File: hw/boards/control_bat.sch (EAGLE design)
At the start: 17 parts, among them U1 579-MCP1703T-3002ECB, U2 771-LPC824M201JDH20J, U3 888-XB24CZ7PIS-004

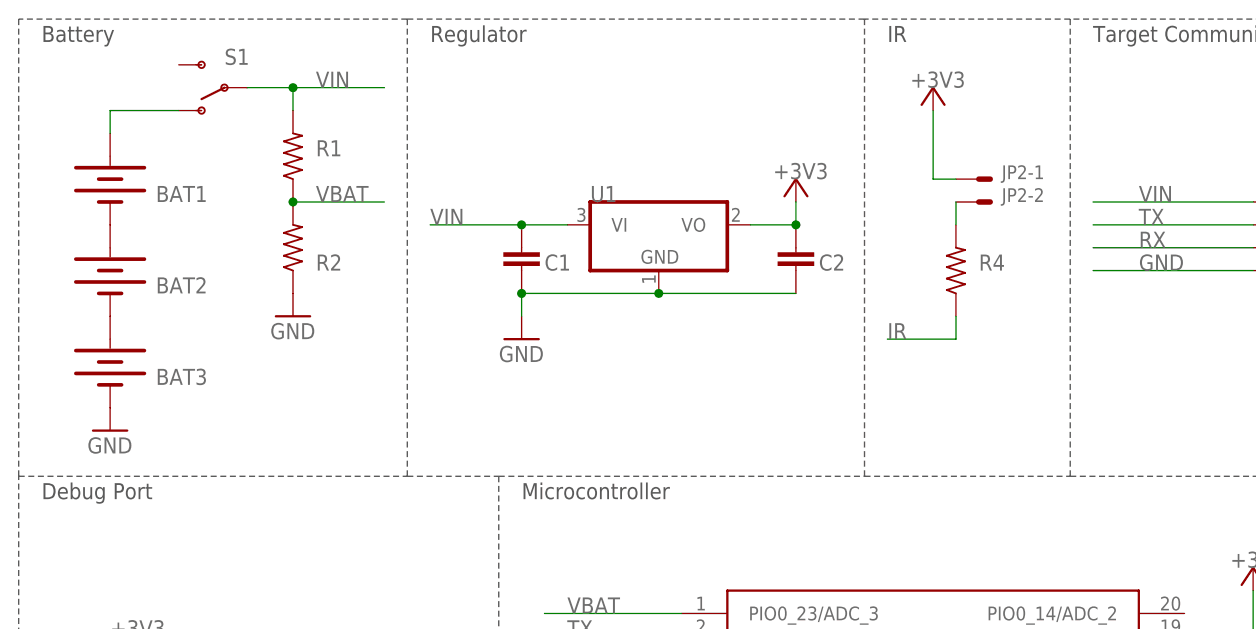
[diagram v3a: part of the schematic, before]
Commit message: Final fixes to the controller board.
This board will probably never be fabbed but I'm documenting the fixes made to hardware here for future reference.
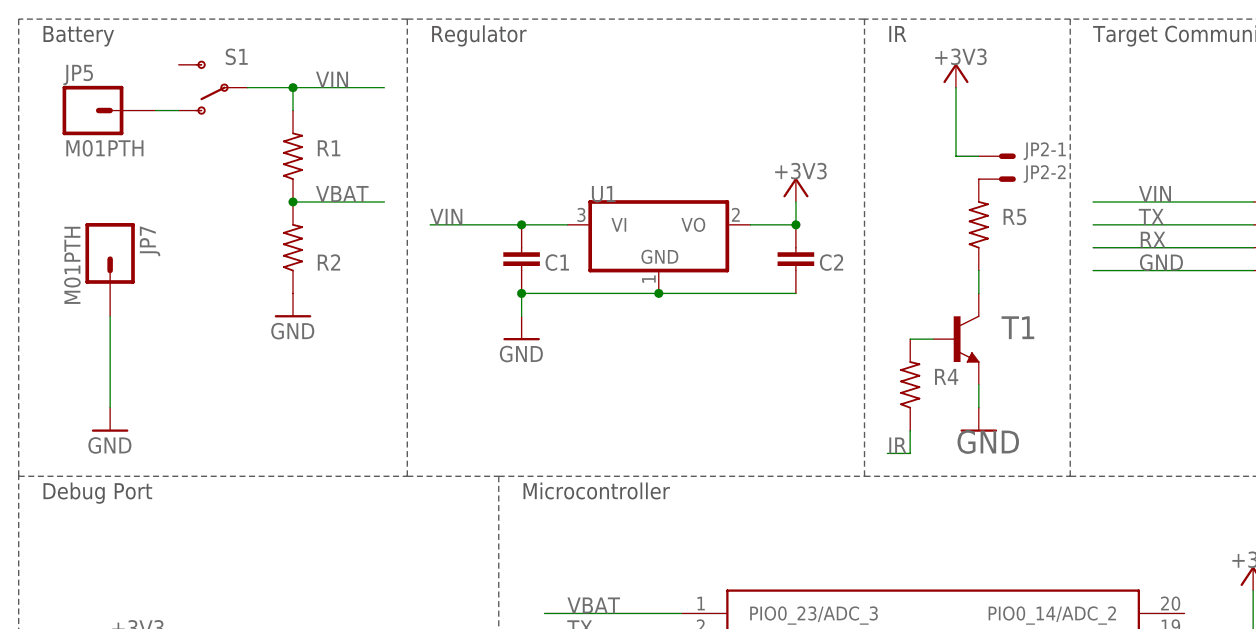
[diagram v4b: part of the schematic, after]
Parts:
- removed BAT1, BAT2, BAT3: 534-082, SparkFun-Electromechanical:BATTERYAAA-KIT
- added JP5, JP7: M01PTH, SparkFun-Connectors:M01PTH
- added R5: 71-CRCW0603-5.6-E3, rcl:R-US_R0603
- added T1: PMBT4401,215, transistor:MMBT4401LT1-NPN-SOT23-BEC
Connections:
- removed net N$2: BAT1.-, BAT2.+
- removed net N$3: BAT1.+, S1.O
- new net N$5: R5.1, T1.C
- new net N$6: R4.2, T1.B
- net GND: now also JP7.1, T1.E; no longer BAT3.-
- net N$1: now also JP5.1, S1.O; no longer BAT2.-, BAT3.+
- net N$4: now also R5.2; no longer R4.2
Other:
- moved on the sheet: JP2-1, JP2-2, R4
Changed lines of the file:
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@@
 <setting verticaltext="up"/>
 </settings>
-<grid distance="0.1" unitdist="inch" unit="inch" style="lines" multiple="1" display="no" altdistance="0.01" altunitdist="inch" altunit="inch"/>
+<grid distance="0.1" unitdist="inch" unit="inch" style="lines" multiple="1" display="yes" altdistance="0.01" altunitdist="inch" altunit="inch"/>
 <layers>
 <layer number="1" name="Top" color="4" fill="1" visible="no" active="no"/>
@@
 <part name="JP3" library="con-molex" deviceset="53?-04" device="398" value="798-DF134P125V20"/>
 <part name="JP1" library="torpedo" deviceset="FTSH-105" device="" value="FTSH-105-01-L"/>
-<part name="BAT3" library="SparkFun-Electromechanical" deviceset="BATTERY" device="AAA-KIT" value="534-082"/>
 <part name="U3" library="xbee" deviceset="XBEE-SMT" device="" value="888-XB24CZ7PIS-004"/>
-<part name="BAT2" library="SparkFun-Electromechanical" deviceset="BATTERY" device="AAA-KIT" value="534-082"/>
-<part name="BAT1" library="SparkFun-Electromechanical" deviceset="BATTERY" device="AAA-KIT" value="534-082"/>
 <part name="GND1" library="supply1" deviceset="GND" device=""/>
 <part name="+3V35" library="supply1" deviceset="+3V3" device=""/>
@@
 <part name="R3" library="rcl" deviceset="R-US_" device="R0603" value="71-CRCW0603-10K-E3"/>
 <part name="JP2" library="con-molex" deviceset="53?-02" device="398" value="798-DF132P125V20"/>
+<part name="T1" library="transistor" deviceset="*-NPN-" device="SOT23-BEC" technology="MMBT4401LT1" value="PMBT4401,215"/>
+<part name="GND8" library="supply1" deviceset="GND" device=""/>
+<part name="R5" library="rcl" deviceset="R-US_" device="R0603" value="71-CRCW0603-5.6-E3"/>
+<part name="JP5" library="SparkFun-Connectors" deviceset="M01" device="PTH"/>
+<part name="JP7" library="SparkFun-Connectors" deviceset="M01" device="PTH"/>
 </parts>
 <sheets>
@@
 <attribute name="NAME" x="238.76" y="35.56" size="1.778" layer="95"/>
 </instance>
-<instance part="BAT3" gate="G$1" x="223.52" y="71.12" smashed="yes" rot="R270">
-<attribute name="NAME" x="228.6" y="68.58" size="1.778" layer="95"/>
-</instance>
 <instance part="U3" gate="G$1" x="393.7" y="58.42" smashed="yes">
 <attribute name="NAME" x="381" y="86.36" size="1.778" layer="95" font="vector"/>
-</instance>
-<instance part="BAT2" gate="G$1" x="223.52" y="81.28" smashed="yes" rot="R270">
-<attribute name="NAME" x="228.6" y="78.74" size="1.778" layer="95"/>
-</instance>
-<instance part="BAT1" gate="G$1" x="223.52" y="91.44" smashed="yes" rot="R270">
-<attribute name="NAME" x="228.6" y="88.9" size="1.778" layer="95"/>
 </instance>
 <instance part="GND1" gate="1" x="223.52" y="63.5" smashed="yes">
@@
 <attribute name="VALUE" x="383.54" y="5.08" size="1.778" layer="96"/>
 </instance>
-<instance part="+3V33" gate="G$1" x="314.96" y="101.6" smashed="yes">
-<attribute name="VALUE" x="312.42" y="101.6" size="1.778" layer="96"/>
-</instance>
-<instance part="R4" gate="G$1" x="317.5" y="81.28" smashed="yes" rot="R90">
-<attribute name="NAME" x="320.04" y="81.28" size="1.778" layer="95"/>
+<instance part="+3V33" gate="G$1" x="317.5" y="104.14" smashed="yes">
+<attribute name="VALUE" x="314.96" y="104.14" size="1.778" layer="96"/>
+</instance>
+<instance part="R4" gate="G$1" x="312.42" y="68.58" smashed="yes" rot="R90">
+<attribute name="NAME" x="314.96" y="68.58" size="1.778" layer="95"/>
 </instance>
 <instance part="U2" gate="G$1" x="312.42" y="30.48" smashed="yes">
@@
 <attribute name="NAME" x="256.54" y="17.78" size="1.778" layer="95"/>
 </instance>
-<instance part="JP2" gate="-1" x="320.04" y="91.44" smashed="yes">
-<attribute name="NAME" x="322.58" y="91.44" size="1.524" layer="95"/>
-</instance>
-<instance part="JP2" gate="-2" x="320.04" y="88.9" smashed="yes">
-<attribute name="NAME" x="322.58" y="88.9" size="1.524" layer="95"/>
-</instance>
+<instance part="JP2" gate="-1" x="322.58" y="93.98" smashed="yes">
+<attribute name="NAME" x="325.12" y="93.98" size="1.524" layer="95"/>
+</instance>
+<instance part="JP2" gate="-2" x="322.58" y="91.44" smashed="yes">
+<attribute name="NAME" x="325.12" y="91.44" size="1.524" layer="95"/>
+</instance>
+<instance part="T1" gate="G$1" x="317.5" y="73.66" smashed="yes">
+<attribute name="NAME" x="322.58" y="73.66" size="2.54" layer="95"/>
+</instance>
+<instance part="GND8" gate="1" x="320.04" y="63.5" smashed="yes">
+<attribute name="VALUE" x="317.5" y="60.96" size="2.54" layer="96"/>
+</instance>
+<instance part="R5" gate="G$1" x="320.04" y="86.36" smashed="yes" rot="R90">
+<attribute name="NAME" x="322.58" y="86.36" size="1.778" layer="95"/>
+</instance>
+<instance part="JP5" gate="G$1" x="220.98" y="99.06"/>
+<instance part="JP7" gate="G$1" x="223.52" y="83.82" rot="R270"/>
 </instances>
 <busses>
@@
 </segment>
 <segment>
-<pinref part="BAT3" gate="G$1" pin="-"/>
-<pinref part="GND1" gate="1" pin="GND"/>
-</segment>
-<segment>
 <pinref part="GND6" gate="1" pin="GND"/>
 <wire x1="375.92" y1="27.94" x2="375.92" y2="30.48" width="0.1524" layer="91"/>
@@
 <junction x="345.44" y="33.02"/>
 </segment>
+<segment>
+<pinref part="T1" gate="G$1" pin="E"/>
+<pinref part="GND8" gate="1" pin="GND"/>
+<wire x1="320.04" y1="68.58" x2="320.04" y2="66.04" width="0.1524" layer="91"/>
+</segment>
+<segment>
+<pinref part="GND1" gate="1" pin="GND"/>
+<pinref part="JP7" gate="G$1" pin="1"/>
+<wire x1="223.52" y1="76.2" x2="223.52" y2="66.04" width="0.1524" layer="91"/>
+</segment>
 </net>
 <net name="+3V3" class="0">
@@
 <segment>
 <pinref part="+3V33" gate="G$1" pin="+3V3"/>
-<wire x1="314.96" y1="99.06" x2="314.96" y2="91.44" width="0.1524" layer="91"/>
-<wire x1="314.96" y1="91.44" x2="317.5" y2="91.44" width="0.1524" layer="91"/>
+<wire x1="317.5" y1="101.6" x2="317.5" y2="93.98" width="0.1524" layer="91"/>
+<wire x1="317.5" y1="93.98" x2="320.04" y2="93.98" width="0.1524" layer="91"/>
 <pinref part="JP2" gate="-1" pin="S"/>
 </segment>
@@
 </segment>
 </net>
-<net name="N$1" class="0">
-<segment>
-<pinref part="BAT3" gate="G$1" pin="+"/>
-<pinref part="BAT2" gate="G$1" pin="-"/>
-</segment>
-</net>
-<net name="N$2" class="0">
-<segment>
-<pinref part="BAT2" gate="G$1" pin="+"/>
-<pinref part="BAT1" gate="G$1" pin="-"/>
-</segment>
-</net>
 <net name="RF_TX" class="0">
 <segment>
@@
 </segment>
 </net>
-<net name="N$3" class="0">
-<segment>
-<pinref part="BAT1" gate="G$1" pin="+"/>
-<pinref part="S1" gate="1" pin="O"/>
-<wire x1="223.52" y1="96.52" x2="223.52" y2="99.06" width="0.1524" layer="91"/>
-<wire x1="223.52" y1="99.06" x2="231.14" y2="99.06" width="0.1524" layer="91"/>
-</segment>
-</net>
-<net name="N$4" class="0">
-<segment>
-<pinref part="R4" gate="G$1" pin="2"/>
-<wire x1="317.5" y1="88.9" x2="317.5" y2="86.36" width="0.1524" layer="91"/>
-<pinref part="JP2" gate="-2" pin="S"/>
-</segment>
-</net>
 <net name="IR" class="0">
 <segment>
 <pinref part="R4" gate="G$1" pin="1"/>
-<wire x1="317.5" y1="76.2" x2="317.5" y2="73.66" width="0.1524" layer="91"/>
-<wire x1="317.5" y1="73.66" x2="309.88" y2="73.66" width="0.1524" layer="91"/>
-<label x="309.88" y="73.66" size="1.778" layer="95"/>
+<wire x1="312.42" y1="63.5" x2="312.42" y2="60.96" width="0.1524" layer="91"/>
+<wire x1="312.42" y1="60.96" x2="309.88" y2="60.96" width="0.1524" layer="91"/>
+<label x="309.88" y="60.96" size="1.778" layer="95"/>
 </segment>
 <segment>
@@
 </segment>
 </net>
+<net name="N$5" class="0">
+<segment>
+<pinref part="T1" gate="G$1" pin="C"/>
+<pinref part="R5" gate="G$1" pin="1"/>
+<wire x1="320.04" y1="81.28" x2="320.04" y2="78.74" width="0.1524" layer="91"/>
+</segment>
+</net>
+<net name="N$4" class="0">
+<segment>
+<pinref part="R5" gate="G$1" pin="2"/>
+<pinref part="JP2" gate="-2" pin="S"/>
+</segment>
+</net>
+<net name="N$6" class="0">
+<segment>
+<pinref part="R4" gate="G$1" pin="2"/>
+<pinref part="T1" gate="G$1" pin="B"/>
+<wire x1="312.42" y1="73.66" x2="314.96" y2="73.66" width="0.1524" layer="91"/>
+</segment>
+</net>
+<net name="N$1" class="0">
+<segment>
+<pinref part="JP5" gate="G$1" pin="1"/>
+<pinref part="S1" gate="1" pin="O"/>
+<wire x1="228.6" y1="99.06" x2="231.14" y2="99.06" width="0.1524" layer="91"/>
+</segment>
+</net>
